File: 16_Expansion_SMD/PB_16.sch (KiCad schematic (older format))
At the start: 10 parts, among them J17 Power In Left, J18 Power In Right, J19 Expansion Header, J20 v4 Input

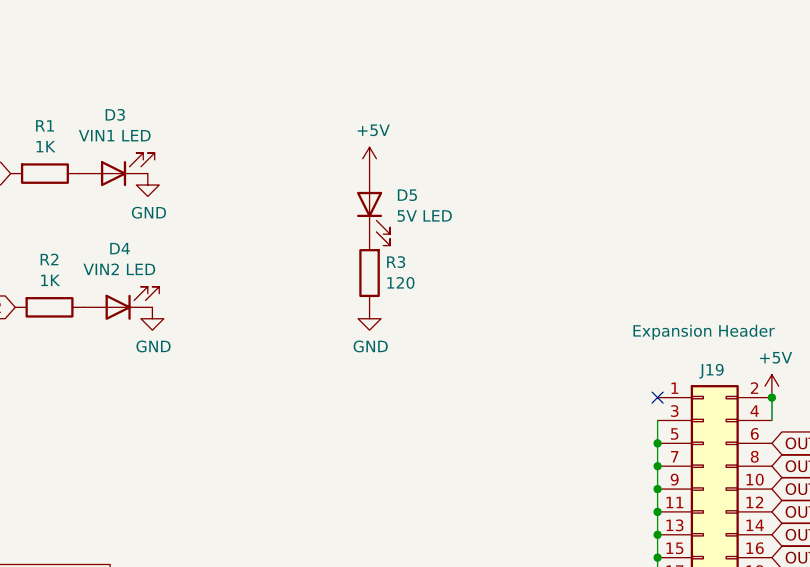
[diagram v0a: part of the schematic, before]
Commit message: added BOM and Position file for SMD assembly
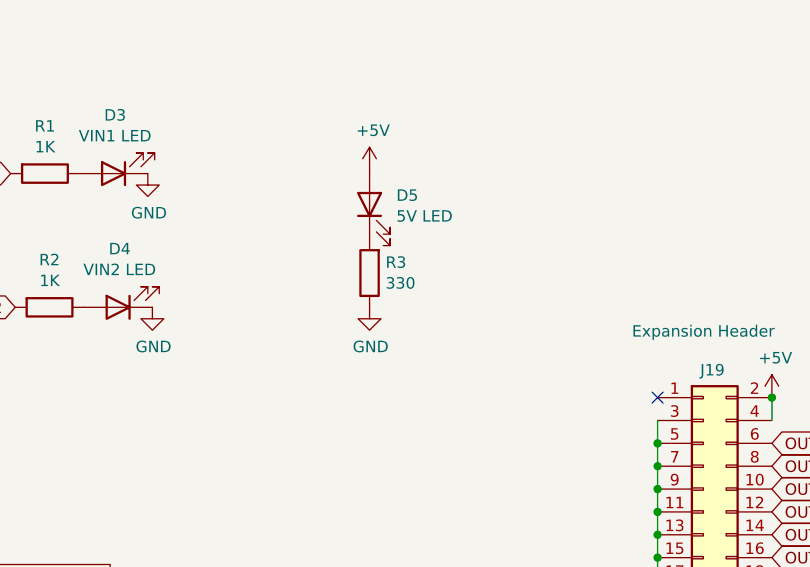
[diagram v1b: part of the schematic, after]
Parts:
- D3, D4, D5: Digi-Key_PN 754-1217-ND -> 732-4986-1-ND; LCSC (none) -> C2297; MPN WP3A8GD -> 150080VS75000
- R1, R2: Digi-Key_PN CF14JT1K00CT-ND -> 311-1.00KCRCT-ND; LCSC (none) -> C17513; MPN CF14JT1K00 -> RC0805FR-071KL
- R3: value 120 -> 330; Digi-Key_PN CF14JT120RCT-ND -> 311-330CRCT-ND; LCSC (none) -> C17630; MPN CF14JT120R -> RC0805FR-07330RL
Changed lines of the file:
@@
 F 2 "LED_SMD:LED_0805_2012Metric_Pad1.15x1.40mm_HandSolder" H 5905 2405 50  0001 C CNN
 F 3 "~" H 5905 2405 50  0001 C CNN
-F 4 "754-1217-ND" H 5905 2405 50  0001 C CNN "Digi-Key_PN"
-F 5 "WP3A8GD" H 5905 2405 50  0001 C CNN "MPN"
+F 4 "732-4986-1-ND" H 5905 2405 50  0001 C CNN "Digi-Key_PN"
+F 5 "150080VS75000" H 5905 2405 50  0001 C CNN "MPN"
+F 6 "C2297" H 5905 2405 50  0001 C CNN "LCSC"
 	1    5905 2405
 	-1   0    0    1
@@
 F 2 "Resistor_SMD:R_0805_2012Metric_Pad1.15x1.40mm_HandSolder" V 5535 2405 50  0001 C CNN
 F 3 "~" H 5605 2405 50  0001 C CNN
-F 4 "CF14JT1K00CT-ND" H 5605 2405 50  0001 C CNN "Digi-Key_PN"
-F 5 "CF14JT1K00" H 5605 2405 50  0001 C CNN "MPN"
+F 4 "311-1.00KCRCT-ND" H 5605 2405 50  0001 C CNN "Digi-Key_PN"
+F 5 "RC0805FR-071KL" H 5605 2405 50  0001 C CNN "MPN"
+F 6 "C17513" H 5605 2405 50  0001 C CNN "LCSC"
 	1    5605 2405
 	0    1    1    0
@@
 F 2 "Resistor_SMD:R_0805_2012Metric_Pad1.15x1.40mm_HandSolder" V 5555 2990 50  0001 C CNN
 F 3 "~" H 5625 2990 50  0001 C CNN
-F 4 "CF14JT1K00CT-ND" H 5625 2990 50  0001 C CNN "Digi-Key_PN"
-F 5 "CF14JT1K00" H 5625 2990 50  0001 C CNN "MPN"
+F 4 "311-1.00KCRCT-ND" H 5625 2990 50  0001 C CNN "Digi-Key_PN"
+F 5 "RC0805FR-071KL" H 5625 2990 50  0001 C CNN "MPN"
+F 6 "C17513" H 5625 2990 50  0001 C CNN "LCSC"
 	1    5625 2990
 	0    1    1    0
@@
 P 7025 2840
 F 0 "R3" H 6955 2794 50  0000 R CNN
-F 1 "120" H 6955 2885 50  0000 R CNN
+F 1 "330" H 6955 2885 50  0000 R CNN
 F 2 "Resistor_SMD:R_0805_2012Metric_Pad1.15x1.40mm_HandSolder" V 6955 2840 50  0001 C CNN
 F 3 "~" H 7025 2840 50  0001 C CNN
-F 4 "CF14JT120RCT-ND" H 7025 2840 50  0001 C CNN "Digi-Key_PN"
-F 5 "CF14JT120R" H 7025 2840 50  0001 C CNN "MPN"
+F 4 "311-330CRCT-ND" H 7025 2840 50  0001 C CNN "Digi-Key_PN"
+F 5 "RC0805FR-07330RL" H 7025 2840 50  0001 C CNN "MPN"
+F 6 "C17630" H 7025 2840 50  0001 C CNN "LCSC"
 	1    7025 2840
 	-1   0    0    1
@@
 F 2 "LED_SMD:LED_0805_2012Metric_Pad1.15x1.40mm_HandSolder" H 5925 2990 50  0001 C CNN
 F 3 "~" H 5925 2990 50  0001 C CNN
-F 4 "754-1217-ND" H 5925 2990 50  0001 C CNN "Digi-Key_PN"
-F 5 "WP3A8GD" H 5925 2990 50  0001 C CNN "MPN"
+F 4 "732-4986-1-ND" H 5925 2990 50  0001 C CNN "Digi-Key_PN"
+F 5 "150080VS75000" H 5925 2990 50  0001 C CNN "MPN"
+F 6 "C2297" H 5925 2990 50  0001 C CNN "LCSC"
 	1    5925 2990
 	-1   0    0    1
@@
 F 2 "LED_SMD:LED_0805_2012Metric_Pad1.15x1.40mm_HandSolder" H 7025 2540 50  0001 C CNN
 F 3 "~" H 7025 2540 50  0001 C CNN
-F 4 "754-1217-ND" H 7025 2540 50  0001 C CNN "Digi-Key_PN"
-F 5 "WP3A8GD" H 7025 2540 50  0001 C CNN "MPN"
+F 4 "732-4986-1-ND" H 7025 2540 50  0001 C CNN "Digi-Key_PN"
+F 5 "150080VS75000" H 7025 2540 50  0001 C CNN "MPN"
+F 6 "C2297" H 7025 2540 50  0001 C CNN "LCSC"
 	1    7025 2540
 	0    -1   -1   0
